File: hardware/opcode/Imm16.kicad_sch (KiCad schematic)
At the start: 4 parts, among them U18 74HC597, U19 74HC597

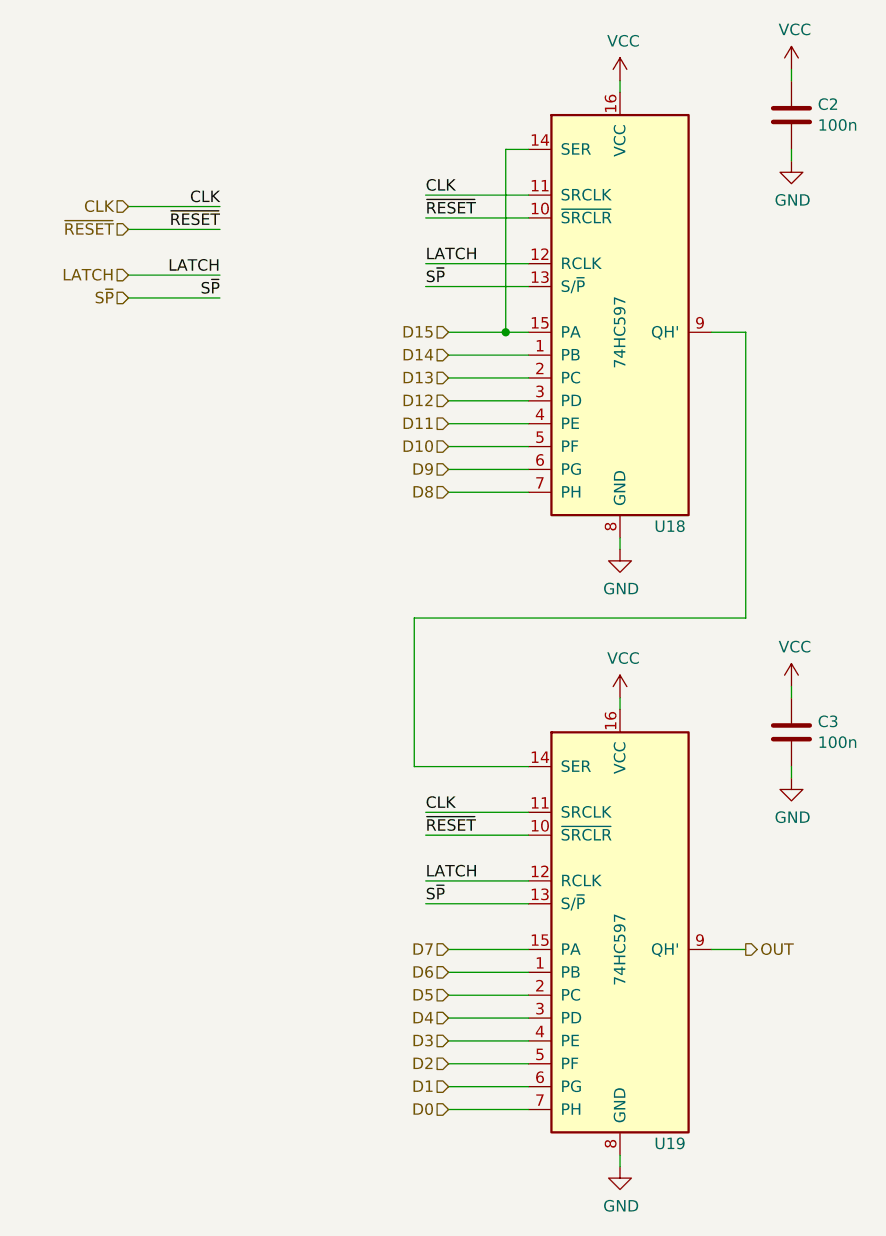
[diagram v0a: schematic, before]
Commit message: Update all to Kicad 6
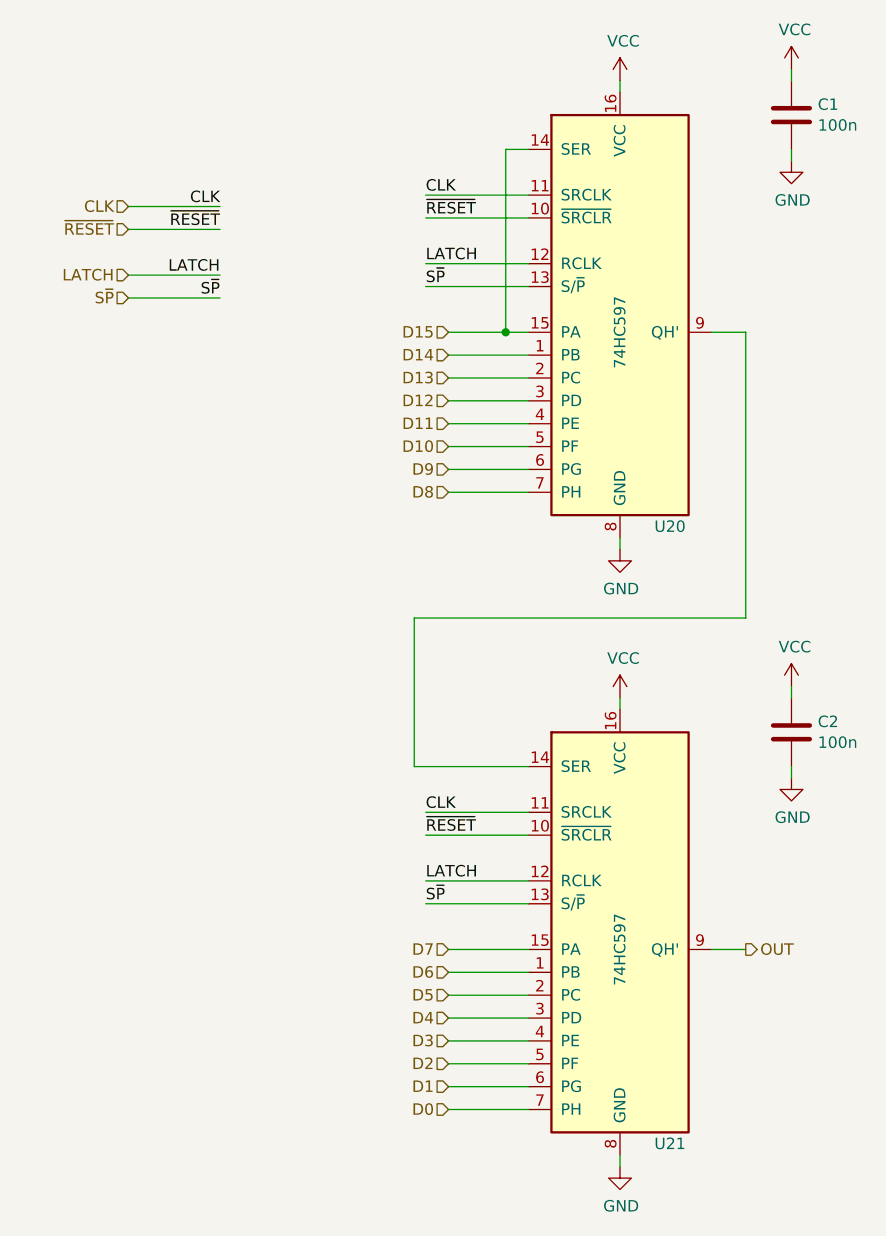
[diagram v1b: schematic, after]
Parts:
- renumbered C2 to C1, C3 to C2, U18 to U20, U19 to U21
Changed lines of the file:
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@@
   (symbol (lib_id "power:VCC") (at 106.68 50.8 0)
     (in_bom yes) (on_board yes)
-    (property "Reference" "#PWR0139" (id 0) (at 106.68 54.61 0)
+    (property "Reference" "#PWR066" (id 0) (at 106.68 54.61 0)
       (effects (font (size 1.27 1.27)) hide)
     )
@@
   (symbol (lib_id "power:GND") (at 106.68 60.96 0)
     (in_bom yes) (on_board yes)
-    (property "Reference" "#PWR0140" (id 0) (at 106.68 67.31 0)
+    (property "Reference" "#PWR068" (id 0) (at 106.68 67.31 0)
       (effects (font (size 1.27 1.27)) hide)
     )
@@
   (symbol (lib_id "power:GND") (at 106.68 129.54 0)
     (in_bom yes) (on_board yes)
-    (property "Reference" "#PWR0144" (id 0) (at 106.68 135.89 0)
+    (property "Reference" "#PWR072" (id 0) (at 106.68 135.89 0)
       (effects (font (size 1.27 1.27)) hide)
     )
@@
   (symbol (lib_id "power:GND") (at 87.63 104.14 0)
     (in_bom yes) (on_board yes)
-    (property "Reference" "#PWR0138" (id 0) (at 87.63 110.49 0)
+    (property "Reference" "#PWR069" (id 0) (at 87.63 110.49 0)
       (effects (font (size 1.27 1.27)) hide)
     )
@@
   (symbol (lib_id "riscv-serial:74HC597") (at 87.63 80.01 0)
     (in_bom yes) (on_board yes)
-    (property "Reference" "U18" (id 0) (at 91.44 101.6 0)
+    (property "Reference" "U20" (id 0) (at 91.44 101.6 0)
       (effects (font (size 1.27 1.27)) (justify left))
     )
@@
   (symbol (lib_id "power:VCC") (at 87.63 52.07 0)
     (in_bom yes) (on_board yes)
-    (property "Reference" "#PWR0137" (id 0) (at 87.63 55.88 0)
+    (property "Reference" "#PWR067" (id 0) (at 87.63 55.88 0)
       (effects (font (size 1.27 1.27)) hide)
     )
@@
   (symbol (lib_id "Device:C") (at 106.68 55.88 0)
     (in_bom yes) (on_board yes)
-    (property "Reference" "C2" (id 0) (at 109.601 54.7116 0)
+    (property "Reference" "C1" (id 0) (at 109.601 54.7116 0)
       (effects (font (size 1.27 1.27)) (justify left))
     )
@@
   (symbol (lib_id "riscv-serial:74HC597") (at 87.63 148.59 0)
     (in_bom yes) (on_board yes)
-    (property "Reference" "U19" (id 0) (at 91.44 170.18 0)
+    (property "Reference" "U21" (id 0) (at 91.44 170.18 0)
       (effects (font (size 1.27 1.27)) (justify left))
     )
@@
   (symbol (lib_id "power:VCC") (at 87.63 120.65 0)
     (in_bom yes) (on_board yes)
-    (property "Reference" "#PWR0141" (id 0) (at 87.63 124.46 0)
+    (property "Reference" "#PWR071" (id 0) (at 87.63 124.46 0)
       (effects (font (size 1.27 1.27)) hide)
     )
@@
   (symbol (lib_id "power:GND") (at 87.63 172.72 0)
     (in_bom yes) (on_board yes)
-    (property "Reference" "#PWR0142" (id 0) (at 87.63 179.07 0)
+    (property "Reference" "#PWR073" (id 0) (at 87.63 179.07 0)
       (effects (font (size 1.27 1.27)) hide)
     )
@@
   (symbol (lib_id "Device:C") (at 106.68 124.46 0)
     (in_bom yes) (on_board yes)
-    (property "Reference" "C3" (id 0) (at 109.601 123.2916 0)
+    (property "Reference" "C2" (id 0) (at 109.601 123.2916 0)
       (effects (font (size 1.27 1.27)) (justify left))
     )
@@
   (symbol (lib_id "power:VCC") (at 106.68 119.38 0)
     (in_bom yes) (on_board yes)
-    (property "Reference" "#PWR0143" (id 0) (at 106.68 123.19 0)
+    (property "Reference" "#PWR070" (id 0) (at 106.68 123.19 0)
       (effects (font (size 1.27 1.27)) hide)
     )

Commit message: Updated schematics and pcbs
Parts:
- renumbered C2 to C10, C1 to C9, U20 to U28, U21 to U29
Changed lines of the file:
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@@
   (symbol (lib_id "power:VCC") (at 106.68 50.8 0)
     (in_bom yes) (on_board yes)
-    (property "Reference" "#PWR066" (id 0) (at 106.68 54.61 0)
+    (property "Reference" "#PWR0128" (id 0) (at 106.68 54.61 0)
       (effects (font (size 1.27 1.27)) hide)
     )
@@
   (symbol (lib_id "power:GND") (at 106.68 60.96 0)
     (in_bom yes) (on_board yes)
-    (property "Reference" "#PWR068" (id 0) (at 106.68 67.31 0)
+    (property "Reference" "#PWR0130" (id 0) (at 106.68 67.31 0)
       (effects (font (size 1.27 1.27)) hide)
     )
@@
   (symbol (lib_id "power:GND") (at 106.68 129.54 0)
     (in_bom yes) (on_board yes)
-    (property "Reference" "#PWR072" (id 0) (at 106.68 135.89 0)
+    (property "Reference" "#PWR0134" (id 0) (at 106.68 135.89 0)
       (effects (font (size 1.27 1.27)) hide)
     )
@@
   (symbol (lib_id "power:GND") (at 87.63 104.14 0)
     (in_bom yes) (on_board yes)
-    (property "Reference" "#PWR069" (id 0) (at 87.63 110.49 0)
+    (property "Reference" "#PWR0131" (id 0) (at 87.63 110.49 0)
       (effects (font (size 1.27 1.27)) hide)
     )
@@
   (symbol (lib_id "riscv-serial:74HC597") (at 87.63 80.01 0)
     (in_bom yes) (on_board yes)
-    (property "Reference" "U20" (id 0) (at 91.44 101.6 0)
+    (property "Reference" "U28" (id 0) (at 91.44 101.6 0)
       (effects (font (size 1.27 1.27)) (justify left))
     )
@@
   (symbol (lib_id "power:VCC") (at 87.63 52.07 0)
     (in_bom yes) (on_board yes)
-    (property "Reference" "#PWR067" (id 0) (at 87.63 55.88 0)
+    (property "Reference" "#PWR0129" (id 0) (at 87.63 55.88 0)
       (effects (font (size 1.27 1.27)) hide)
     )
@@
   (symbol (lib_id "Device:C") (at 106.68 55.88 0)
     (in_bom yes) (on_board yes)
-    (property "Reference" "C1" (id 0) (at 109.601 54.7116 0)
+    (property "Reference" "C9" (id 0) (at 109.601 54.7116 0)
       (effects (font (size 1.27 1.27)) (justify left))
     )
@@
   (symbol (lib_id "riscv-serial:74HC597") (at 87.63 148.59 0)
     (in_bom yes) (on_board yes)
-    (property "Reference" "U21" (id 0) (at 91.44 170.18 0)
+    (property "Reference" "U29" (id 0) (at 91.44 170.18 0)
       (effects (font (size 1.27 1.27)) (justify left))
     )
@@
   (symbol (lib_id "power:VCC") (at 87.63 120.65 0)
     (in_bom yes) (on_board yes)
-    (property "Reference" "#PWR071" (id 0) (at 87.63 124.46 0)
+    (property "Reference" "#PWR0133" (id 0) (at 87.63 124.46 0)
       (effects (font (size 1.27 1.27)) hide)
     )
@@
   (symbol (lib_id "power:GND") (at 87.63 172.72 0)
     (in_bom yes) (on_board yes)
-    (property "Reference" "#PWR073" (id 0) (at 87.63 179.07 0)
+    (property "Reference" "#PWR0135" (id 0) (at 87.63 179.07 0)
       (effects (font (size 1.27 1.27)) hide)
     )
@@
   (symbol (lib_id "Device:C") (at 106.68 124.46 0)
     (in_bom yes) (on_board yes)
-    (property "Reference" "C2" (id 0) (at 109.601 123.2916 0)
+    (property "Reference" "C10" (id 0) (at 109.601 123.2916 0)
       (effects (font (size 1.27 1.27)) (justify left))
     )
@@
   (symbol (lib_id "power:VCC") (at 106.68 119.38 0)
     (in_bom yes) (on_board yes)
-    (property "Reference" "#PWR070" (id 0) (at 106.68 123.19 0)
+    (property "Reference" "#PWR0132" (id 0) (at 106.68 123.19 0)
       (effects (font (size 1.27 1.27)) hide)
     )
